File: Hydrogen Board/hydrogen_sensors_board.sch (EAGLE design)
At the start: 42 parts, among them U1 ATMEGA328P_TQFP, Y1 16MHz

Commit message: update
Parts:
- removed F3, F4: (no value), polyfuse:POLYFUSE
- removed U$4: RJ9PTH, SparkFun-Connectors:RJ9PTH
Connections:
- removed net N$12: F3.1, U$4.4
- removed net N$14: F4.1, U$4.3
- net +12V: now also ETH1.6; no longer F3.2
- net +5V: now also ETH1.8; no longer F4.2
- net GND: no longer U$4.1, U$4.2
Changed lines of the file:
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@@
 <?xml version="1.0" encoding="utf-8"?>
 <!DOCTYPE eagle SYSTEM "eagle.dtd">
-<eagle version="7.7.0">
+<eagle version="7.4.0">
 <drawing>
 <settings>
@@
 <part name="R11" library="SparkFun-Resistors" deviceset="RESISTOR" device="0603-RES" value="100k"/>
 <part name="R12" library="SparkFun-Resistors" deviceset="RESISTOR" device="0603-RES" value="100k"/>
-<part name="U$4" library="SparkFun-Connectors" deviceset="RJ9" device="PTH"/>
-<part name="F3" library="polyfuse" deviceset="POLYFUSE" device=""/>
-<part name="F4" library="polyfuse" deviceset="POLYFUSE" device=""/>
 <part name="C3" library="adafruit" deviceset="C-US" device="C0603"/>
 <part name="C4" library="adafruit" deviceset="C-US" device="C0603"/>
@@
 <instance part="R11" gate="G$1" x="180.34" y="152.4"/>
 <instance part="R12" gate="G$1" x="180.34" y="149.86"/>
-<instance part="U$4" gate="G$1" x="33.02" y="35.56"/>
-<instance part="F3" gate="G$1" x="43.18" y="40.64"/>
-<instance part="F4" gate="G$1" x="43.18" y="38.1"/>
 <instance part="C3" gate="G$1" x="261.62" y="175.26"/>
 <instance part="C4" gate="G$1" x="254" y="175.26"/>
@@
 <wire x1="234.95" y1="74.93" x2="229.87" y2="74.93" width="0.1524" layer="91"/>
 <label x="229.87" y="74.93" size="1.778" layer="95"/>
-</segment>
-<segment>
-<pinref part="F4" gate="G$1" pin="2"/>
-<wire x1="48.26" y1="38.1" x2="50.8" y2="38.1" width="0.1524" layer="91"/>
-<label x="50.8" y="38.1" size="1.778" layer="95"/>
 </segment>
 <segment>
@@
 <label x="238.76" y="177.8" size="1.778" layer="95"/>
 </segment>
+<segment>
+<pinref part="ETH1" gate="G$1" pin="8"/>
+<wire x1="101.6" y1="33.02" x2="96.52" y2="33.02" width="0.1524" layer="91"/>
+<label x="93.98" y="33.02" size="1.778" layer="95"/>
+</segment>
 </net>
 <net name="GND" class="0">
@@
 <pinref part="ETH1" gate="G$1" pin="5"/>
 <wire x1="101.6" y1="40.64" x2="96.52" y2="40.64" width="0.1524" layer="91"/>
-<label x="96.52" y="40.64" size="1.778" layer="95"/>
-</segment>
-<segment>
-<pinref part="U$4" gate="G$1" pin="2"/>
-<wire x1="38.1" y1="35.56" x2="50.8" y2="35.56" width="0.1524" layer="91"/>
-<label x="50.8" y="35.56" size="1.778" layer="95"/>
-</segment>
-<segment>
-<pinref part="U$4" gate="G$1" pin="1"/>
-<wire x1="38.1" y1="33.02" x2="50.8" y2="33.02" width="0.1524" layer="91"/>
-<label x="50.8" y="33.02" size="1.778" layer="95"/>
+<label x="93.98" y="40.64" size="1.778" layer="95"/>
 </segment>
 <segment>
@@
 </segment>
 <segment>
-<pinref part="F3" gate="G$1" pin="2"/>
-<wire x1="48.26" y1="40.64" x2="50.8" y2="40.64" width="0.1524" layer="91"/>
-<label x="50.8" y="40.64" size="1.778" layer="95"/>
+<pinref part="ETH1" gate="G$1" pin="6"/>
+<wire x1="101.6" y1="38.1" x2="96.52" y2="38.1" width="0.1524" layer="91"/>
+<label x="93.98" y="38.1" size="1.778" layer="95"/>
 </segment>
 </net>
@@
 </segment>
 </net>
-<net name="N$12" class="0">
-<segment>
-<pinref part="U$4" gate="G$1" pin="4"/>
-<pinref part="F3" gate="G$1" pin="1"/>
-</segment>
-</net>
-<net name="N$14" class="0">
-<segment>
-<pinref part="U$4" gate="G$1" pin="3"/>
-<pinref part="F4" gate="G$1" pin="1"/>
-</segment>
-</net>

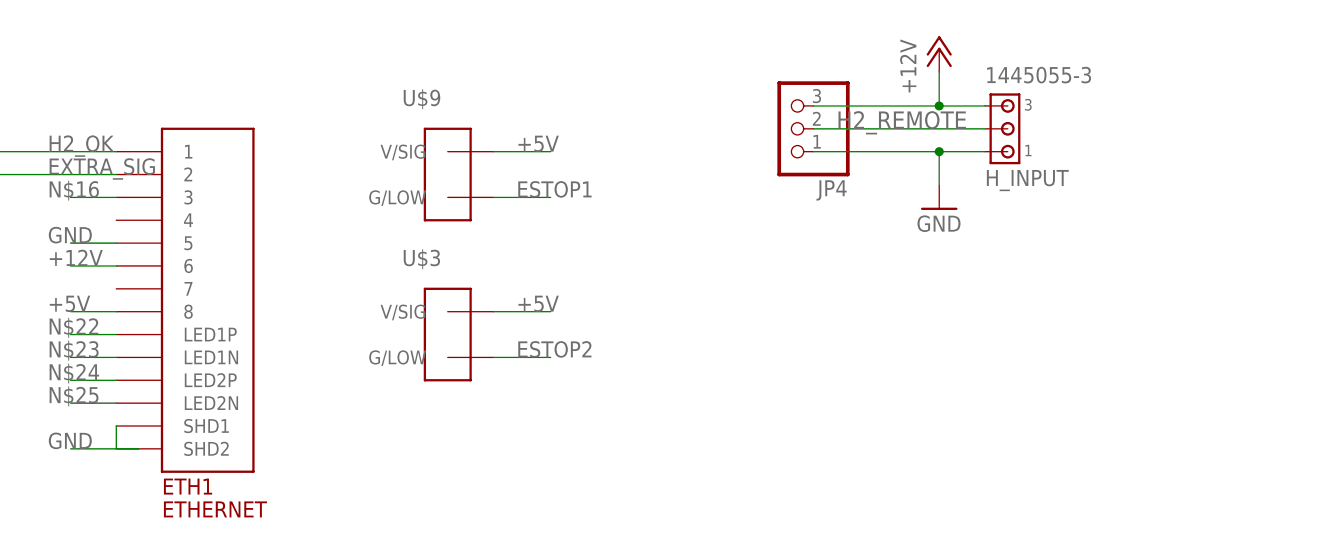
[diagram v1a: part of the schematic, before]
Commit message: cleaned up silk screens
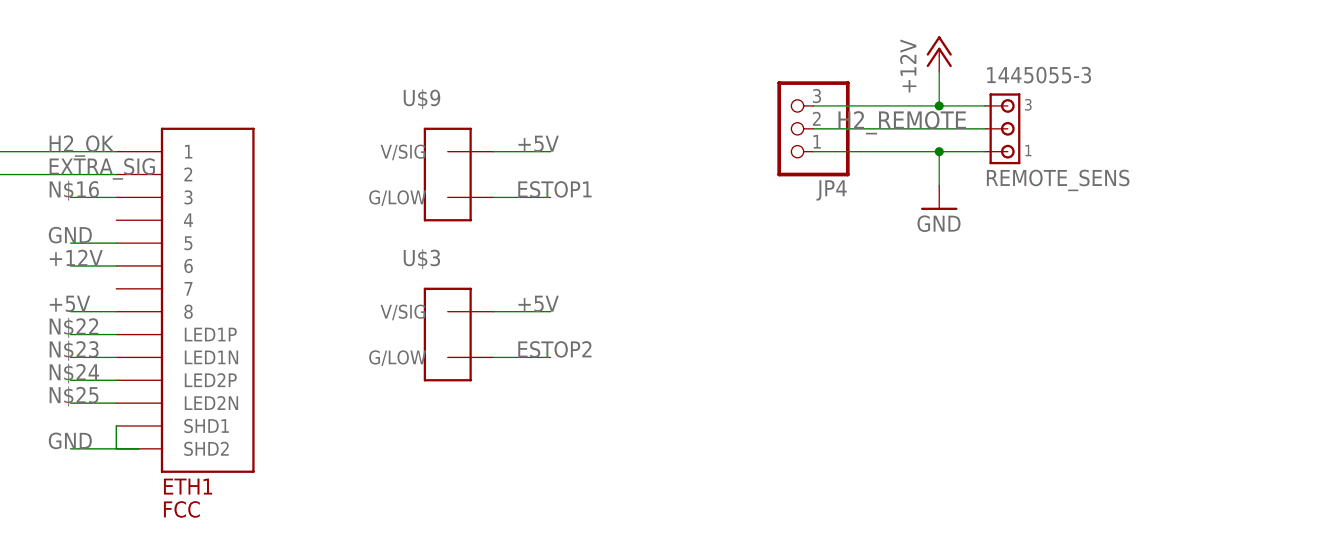
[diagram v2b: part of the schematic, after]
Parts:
- ETH1: value ETHERNET -> FCC
- renumbered H_INPUT to REMOTE_SENS
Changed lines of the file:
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@@
 <?xml version="1.0" encoding="utf-8"?>
 <!DOCTYPE eagle SYSTEM "eagle.dtd">
-<eagle version="7.4.0">
+<eagle version="7.7.0">
 <drawing>
 <settings>
@@
 <part name="H4" library="holes" deviceset="MOUNT-PAD-ROUND" device="3.6" value="MOUNT-PAD-ROUND3.6"/>
 <part name="GND22" library="SparkFun" deviceset="GND" device=""/>
-<part name="ETH1" library="ETHERNET" deviceset="ETHERNET" device=""/>
+<part name="ETH1" library="ETHERNET" deviceset="ETHERNET" device="" value="FCC"/>
 <part name="R5" library="SparkFun-Passives" deviceset="RESISTOR" device="0603-RES" value="10k"/>
 <part name="R6" library="SparkFun-Passives" deviceset="RESISTOR" device="0603-RES" value="10k"/>
@@
 <part name="U$3" library="Shell2013" deviceset="TE770966" device=""/>
 <part name="JP6" library="SparkFun-Connectors" deviceset="FTDI_DEVICE" device=""/>
-<part name="H_INPUT" library="con-amp" deviceset="1445055-3" device=""/>
+<part name="REMOTE_SENS" library="con-amp" deviceset="1445055-3" device=""/>
 <part name="JP4" library="pinhead" deviceset="PINHD-1X3" device=""/>
 <part name="P+12" library="supply1" deviceset="+12V" device=""/>
@@
 <instance part="U$3" gate="G$1" x="135.89" y="30.48" rot="R270"/>
 <instance part="JP6" gate="G$1" x="240.03" y="77.47"/>
-<instance part="H_INPUT" gate="G$1" x="200.66" y="50.8"/>
+<instance part="REMOTE_SENS" gate="G$1" x="200.66" y="50.8"/>
 <instance part="JP4" gate="A" x="176.53" y="53.34" rot="R180"/>
 <instance part="P+12" gate="1" x="193.04" y="62.23"/>
@@
 <segment>
 <pinref part="JP4" gate="A" pin="1"/>
-<pinref part="H_INPUT" gate="G$1" pin="1"/>
+<pinref part="REMOTE_SENS" gate="G$1" pin="1"/>
 <wire x1="179.07" y1="50.8" x2="193.04" y2="50.8" width="0.1524" layer="91"/>
 <wire x1="193.04" y1="50.8" x2="198.12" y2="50.8" width="0.1524" layer="91"/>
@@
 <segment>
 <pinref part="JP4" gate="A" pin="2"/>
-<pinref part="H_INPUT" gate="G$1" pin="2"/>
+<pinref part="REMOTE_SENS" gate="G$1" pin="2"/>
 <wire x1="179.07" y1="53.34" x2="198.12" y2="53.34" width="0.1524" layer="91"/>
 <label x="181.61" y="53.34" size="1.9304" layer="95"/>
@@
 <segment>
 <pinref part="JP4" gate="A" pin="3"/>
-<pinref part="H_INPUT" gate="G$1" pin="3"/>
+<pinref part="REMOTE_SENS" gate="G$1" pin="3"/>
 <wire x1="179.07" y1="55.88" x2="193.04" y2="55.88" width="0.1524" layer="91"/>
 <wire x1="193.04" y1="55.88" x2="198.12" y2="55.88" width="0.1524" layer="91"/>
